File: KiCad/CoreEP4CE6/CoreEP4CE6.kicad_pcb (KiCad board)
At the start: 2 copper layers, 48.6 x 66.3 mm, 12 parts

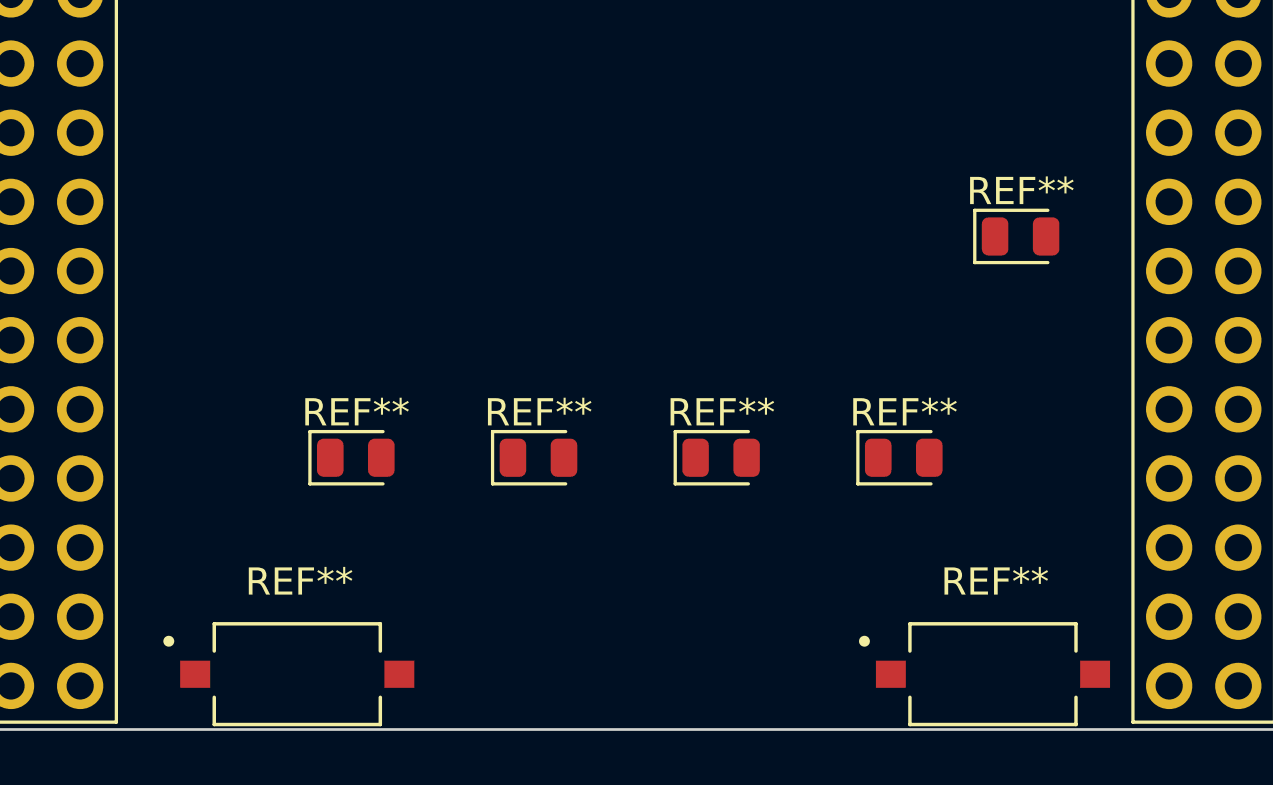
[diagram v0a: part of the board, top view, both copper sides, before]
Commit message: Add light pipes for LED's, tweak opening for on/off switch
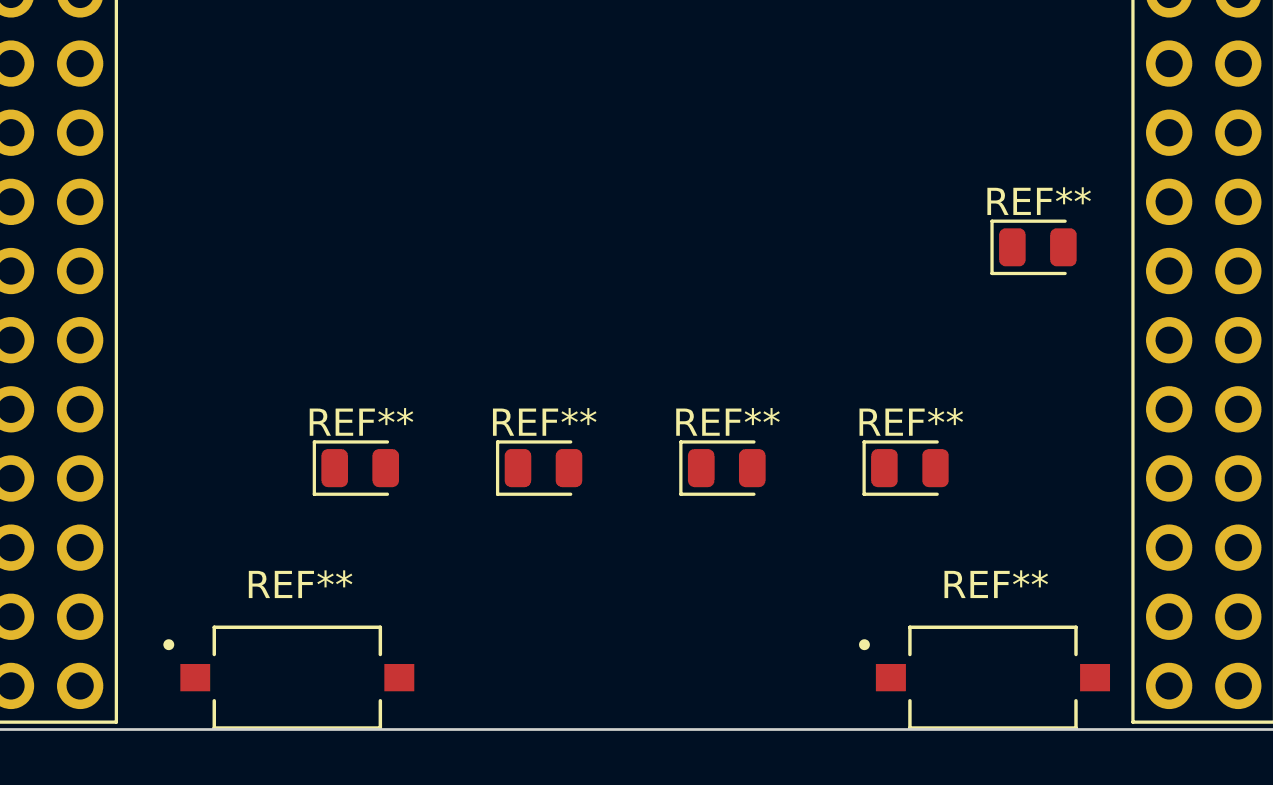
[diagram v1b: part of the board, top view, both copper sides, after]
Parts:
- moved REF** 0.75 mm to (146.9, 103.3)
- moved REF** 0.44 mm to (142.2, 111.4)
- moved REF** 0.43 mm to (135.5, 111.4)
- moved REF** 0.42 mm to (128.8, 111.4)
- moved REF** 0.41 mm to (122.0, 111.4)
- moved REF** 0.13 mm to (119.7, 119.1)
- moved REF** 0.13 mm to (145.3, 119.1)
